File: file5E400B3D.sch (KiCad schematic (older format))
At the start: 12 parts

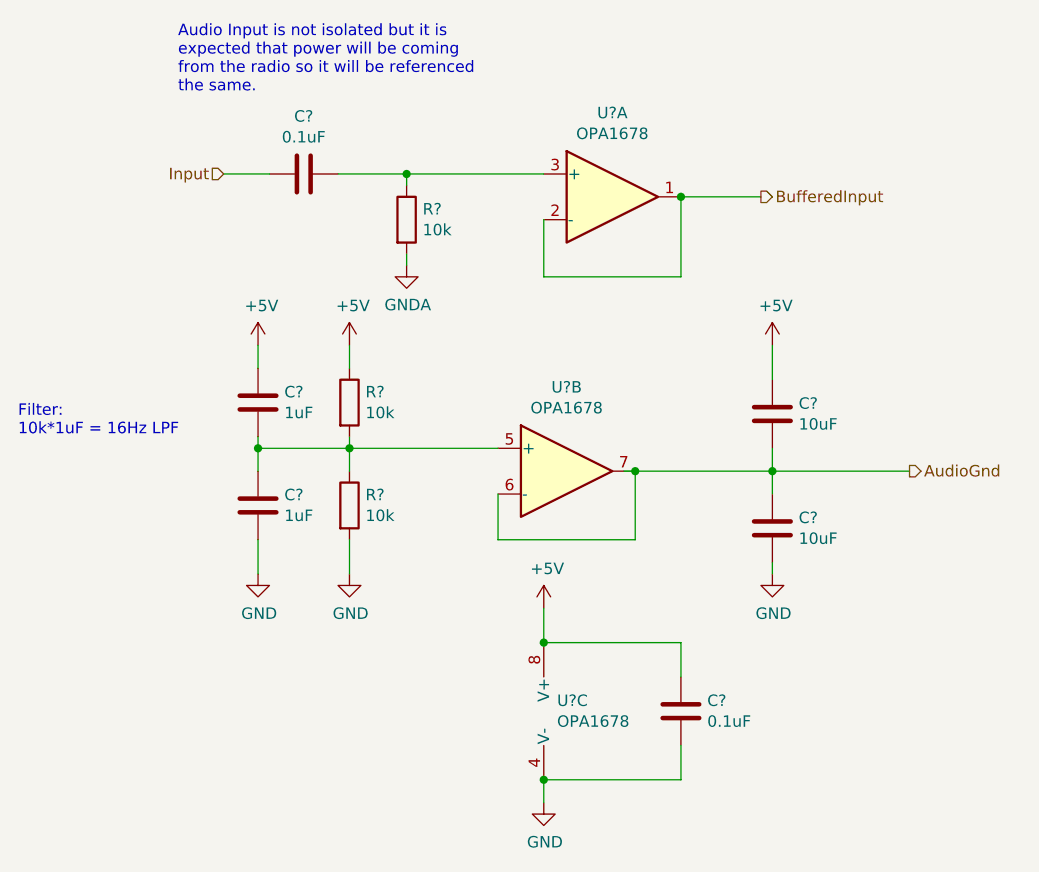
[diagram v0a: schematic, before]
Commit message: Ferrite beads and annotations
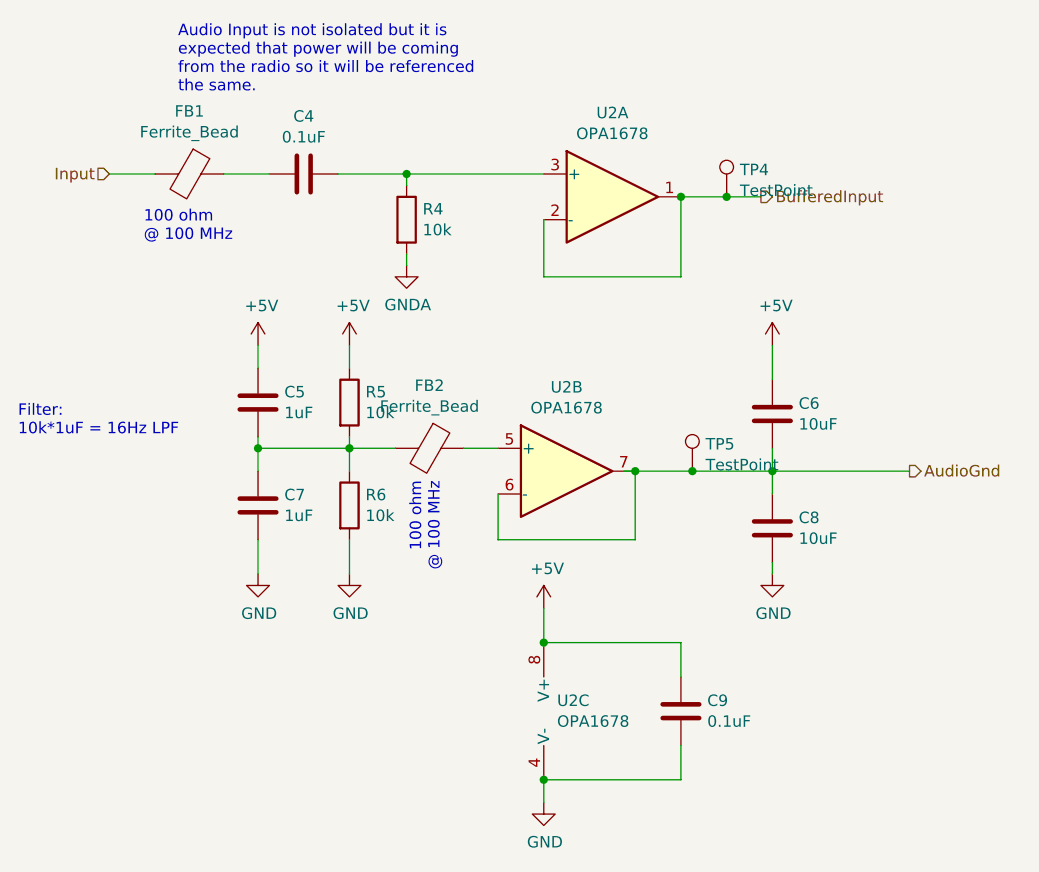
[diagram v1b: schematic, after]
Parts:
- added FB1, FB2: Ferrite_Bead, symbol Device:Ferrite_Bead
- added TP4, TP5: TestPoint, symbol Connector:TestPoint
- gave numbers to parts that had none: 10
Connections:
- wire segments 35 -> 39
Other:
- note added: "100 ohm \n@ 100 MHz"
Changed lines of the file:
@@
 Text HLabel 5900 2600 2    50   Output ~ 0
 BufferedInput
-Text HLabel 3550 2500 0    50   Input ~ 0
+Text HLabel 3050 2500 0    50   Input ~ 0
 Input
 Text HLabel 6550 3800 2    50   Output ~ 0
 AudioGnd
 $Comp
-L Device:R R?
+L Device:R R5
 U 1 1 5E400C47
 P 4100 3500
-F 0 "R?" H 4170 3546 50  0000 L CNN
+F 0 "R5" H 4170 3546 50  0000 L CNN
 F 1 "10k" H 4170 3455 50  0000 L CNN
 F 2 "" V 4030 3500 50  0001 C CNN
@@
 $EndComp
 $Comp
-L Device:R R?
+L Device:R R6
 U 1 1 5E400F84
 P 4100 3950
-F 0 "R?" H 4170 3996 50  0000 L CNN
+F 0 "R6" H 4170 3996 50  0000 L CNN
 F 1 "10k" H 4170 3905 50  0000 L CNN
 F 2 "" V 4030 3950 50  0001 C CNN
@@
 	4100 3650 4100 3700
 $Comp
-L power:+5V #PWR?
+L power:+5V #PWR015
 U 1 1 5E401BE8
 P 4100 3250
-F 0 "#PWR?" H 4100 3100 50  0001 C CNN
+F 0 "#PWR015" H 4100 3100 50  0001 C CNN
 F 1 "+5V" H 4115 3423 50  0000 C CNN
 F 2 "" H 4100 3250 50  0001 C CNN
@@
 $EndComp
 $Comp
-L power:GND #PWR?
+L power:GND #PWR018
 U 1 1 5E4020B9
 P 4100 4250
-F 0 "#PWR?" H 4100 4000 50  0001 C CNN
+F 0 "#PWR018" H 4100 4000 50  0001 C CNN
 F 1 "GND" H 4105 4077 50  0000 C CNN
 F 2 "" H 4100 4250 50  0001 C CNN
@@
 	4100 4250 4100 4100
 $Comp
-L Amplifier_Operational:OPA1678 U?
+L Amplifier_Operational:OPA1678 U2
 U 2 1 5E4026CE
 P 5050 3800
-F 0 "U?" H 5050 4167 50  0000 C CNN
+F 0 "U2" H 5050 4167 50  0000 C CNN
 F 1 "OPA1678" H 5050 4076 50  0000 C CNN
 F 2 "" H 5050 3800 50  0001 C CNN
@@
 $EndComp
 $Comp
-L Amplifier_Operational:OPA1678 U?
+L Amplifier_Operational:OPA1678 U2
 U 1 1 5E40401B
 P 5250 2600
-F 0 "U?" H 5250 2967 50  0000 C CNN
+F 0 "U2" H 5250 2967 50  0000 C CNN
 F 1 "OPA1678" H 5250 2876 50  0000 C CNN
 F 2 "" H 5250 2600 50  0001 C CNN
@@
 $EndComp
 $Comp
-L Amplifier_Operational:OPA1678 U?
+L Amplifier_Operational:OPA1678 U2
 U 3 1 5E405560
 P 5050 4850
-F 0 "U?" H 5008 4896 50  0000 L CNN
+F 0 "U2" H 5008 4896 50  0000 L CNN
 F 1 "OPA1678" H 5008 4805 50  0000 L CNN
 F 2 "" H 5050 4850 50  0001 C CNN
@@
 $EndComp
 $Comp
-L power:+5V #PWR?
+L power:+5V #PWR020
 U 1 1 5E406BA7
 P 4950 4400
-F 0 "#PWR?" H 4950 4250 50  0001 C CNN
+F 0 "#PWR020" H 4950 4250 50  0001 C CNN
 F 1 "+5V" H 4965 4573 50  0000 C CNN
 F 2 "" H 4950 4400 50  0001 C CNN
@@
 $EndComp
 $Comp
-L power:GND #PWR?
+L power:GND #PWR021
 U 1 1 5E406FD4
 P 4950 5250
-F 0 "#PWR?" H 4950 5000 50  0001 C CNN
+F 0 "#PWR021" H 4950 5000 50  0001 C CNN
 F 1 "GND" H 4955 5077 50  0000 C CNN
 F 2 "" H 4950 5250 50  0001 C CNN
@@
 Wire Wire Line
 	4950 4550 4950 4400
-Wire Wire Line
-	4100 3700 4750 3700
 Connection ~ 4100 3700
 Wire Wire Line
@@
 Connection ~ 5350 3800
 Wire Wire Line
-	5550 2600 5900 2600
+	5550 2600 5750 2600
 Wire Wire Line
 	5550 2600 5550 2950
@@
 	4100 3350 4100 3250
 $Comp
-L Device:C C?
+L Device:C C4
 U 1 1 5E450E38
 P 3900 2500
-F 0 "C?" V 3648 2500 50  0000 C CNN
+F 0 "C4" V 3648 2500 50  0000 C CNN
 F 1 "0.1uF" V 3739 2500 50  0000 C CNN
 F 2 "" H 3938 2350 50  0001 C CNN
@@
 	3550 2500 3750 2500
 $Comp
-L power:GNDA #PWR?
+L power:GNDA #PWR013
 U 1 1 5E45287C
 P 4350 2900
-F 0 "#PWR?" H 4350 2650 50  0001 C CNN
+F 0 "#PWR013" H 4350 2650 50  0001 C CNN
 F 1 "GNDA" H 4355 2727 50  0000 C CNN
 F 2 "" H 4350 2900 50  0001 C CNN
@@
 $EndComp
 $Comp
-L Device:C C?
+L Device:C C9
 U 1 1 5E45404C
 P 5550 4850
-F 0 "C?" H 5665 4896 50  0000 L CNN
+F 0 "C9" H 5665 4896 50  0000 L CNN
 F 1 "0.1uF" H 5665 4805 50  0000 L CNN
 F 2 "" H 5588 4700 50  0001 C CNN
@@
 Connection ~ 4950 5150
 $Comp
-L power:+5V #PWR?
+L power:+5V #PWR014
 U 1 1 5E45D063
 P 3700 3250
-F 0 "#PWR?" H 3700 3100 50  0001 C CNN
+F 0 "#PWR014" H 3700 3100 50  0001 C CNN
 F 1 "+5V" H 3715 3423 50  0000 C CNN
 F 2 "" H 3700 3250 50  0001 C CNN
@@
 $EndComp
 $Comp
-L power:GND #PWR?
+L power:GND #PWR017
 U 1 1 5E45D4E7
 P 3700 4250
-F 0 "#PWR?" H 3700 4000 50  0001 C CNN
+F 0 "#PWR017" H 3700 4000 50  0001 C CNN
 F 1 "GND" H 3705 4077 50  0000 C CNN
 F 2 "" H 3700 4250 50  0001 C CNN
@@
 $EndComp
 $Comp
-L Device:C C?
+L Device:C C5
 U 1 1 5E45DB74
 P 3700 3500
-F 0 "C?" H 3815 3546 50  0000 L CNN
+F 0 "C5" H 3815 3546 50  0000 L CNN
 F 1 "1uF" H 3815 3455 50  0000 L CNN
 F 2 "" H 3738 3350 50  0001 C CNN
@@
 $EndComp
 $Comp
-L Device:C C?
+L Device:C C7
 U 1 1 5E45EA2A
 P 3700 3950
-F 0 "C?" H 3815 3996 50  0000 L CNN
+F 0 "C7" H 3815 3996 50  0000 L CNN
 F 1 "1uF" H 3815 3905 50  0000 L CNN
 F 2 "" H 3738 3800 50  0001 C CNN
@@
 Filter:\n10k*1uF = 16Hz LPF
 $Comp
-L Device:C C?
+L Device:C C6
 U 1 1 5E464FDF
 P 5950 3550
-F 0 "C?" H 6065 3596 50  0000 L CNN
+F 0 "C6" H 6065 3596 50  0000 L CNN
 F 1 "10uF" H 6065 3505 50  0000 L CNN
 F 2 "" H 5988 3400 50  0001 C CNN
@@
 $EndComp
 $Comp
-L Device:C C?
+L Device:C C8
 U 1 1 5E4654FA
 P 5950 4050
-F 0 "C?" H 6065 4096 50  0000 L CNN
+F 0 "C8" H 6065 4096 50  0000 L CNN
 F 1 "10uF" H 6065 4005 50  0000 L CNN
 F 2 "" H 5988 3900 50  0001 C CNN
@@
 $EndComp
 $Comp
-L power:+5V #PWR?
+L power:+5V #PWR016
 U 1 1 5E469E13
 P 5950 3250
-F 0 "#PWR?" H 5950 3100 50  0001 C CNN
+F 0 "#PWR016" H 5950 3100 50  0001 C CNN
 F 1 "+5V" H 5965 3423 50  0000 C CNN
 F 2 "" H 5950 3250 50  0001 C CNN
@@
 $EndComp
 $Comp
-L power:GND #PWR?
+L power:GND #PWR019
 U 1 1 5E46A323
 P 5950 4250
-F 0 "#PWR?" H 5950 4000 50  0001 C CNN
+F 0 "#PWR019" H 5950 4000 50  0001 C CNN
 F 1 "GND" H 5955 4077 50  0000 C CNN
 F 2 "" H 5950 4250 50  0001 C CNN
@@
 	5950 3400 5950 3250
 Wire Wire Line
-	5350 3800 5950 3800
+	5350 3800 5600 3800
 Connection ~ 5950 3800
 Wire Wire Line
@@
 	4050 2500 4350 2500
 $Comp
-L Device:R R?
+L Device:R R4
 U 1 1 5E4A8F52
 P 4350 2700
-F 0 "R?" H 4420 2746 50  0000 L CNN
+F 0 "R4" H 4420 2746 50  0000 L CNN
 F 1 "10k" H 4420 2655 50  0000 L CNN
 F 2 "" V 4280 2700 50  0001 C CNN
@@
 Wire Wire Line
 	4350 2850 4350 2900
+$Comp
+L Device:Ferrite_Bead FB1
+U 1 1 5EC0D996
+P 3400 2500
+F 0 "FB1" V 3126 2500 50  0000 C CNN
+F 1 "Ferrite_Bead" V 3217 2500 50  0000 C CNN
+F 2 "" V 3330 2500 50  0001 C CNN
+F 3 "~" H 3400 2500 50  0001 C CNN
+	1    3400 2500
+	0    1    1    0
+$EndComp
+Wire Wire Line
+	3050 2500 3250 2500
+$Comp
+L Device:Ferrite_Bead FB2
+U 1 1 5EC0FD0A
+P 4450 3700
+F 0 "FB2" V 4176 3700 50  0000 C CNN
+F 1 "Ferrite_Bead" V 4267 3700 50  0000 C CNN
+F 2 "" V 4380 3700 50  0001 C CNN
+F 3 "~" H 4450 3700 50  0001 C CNN
+	1    4450 3700
+	0    1    1    0
+$EndComp
+Wire Wire Line
+	4600 3700 4750 3700
+Wire Wire Line
+	4300 3700 4100 3700
+Text Notes 3200 2800 0    50   ~ 0
+100 ohm \n@ 100 MHz
+Text Notes 4500 3850 3    50   ~ 0
+100 ohm \n@ 100 MHz
+$Comp
+L Connector:TestPoint TP4
+U 1 1 5EC17715
+P 5750 2600
+F 0 "TP4" H 5808 2718 50  0000 L CNN
+F 1 "TestPoint" H 5808 2627 50  0000 L CNN
+F 2 "" H 5950 2600 50  0001 C CNN
+F 3 "~" H 5950 2600 50  0001 C CNN
+	1    5750 2600
+	1    0    0    -1
+$EndComp
+Connection ~ 5750 2600
+Wire Wire Line
+	5750 2600 5900 2600
+$Comp
+L Connector:TestPoint TP5
+U 1 1 5EC17DFD
+P 5600 3800
+F 0 "TP5" H 5658 3918 50  0000 L CNN
+F 1 "TestPoint" H 5658 3827 50  0000 L CNN
+F 2 "" H 5800 3800 50  0001 C CNN
+F 3 "~" H 5800 3800 50  0001 C CNN
+	1    5600 3800
+	1    0    0    -1
+$EndComp
+Connection ~ 5600 3800
+Wire Wire Line
+	5600 3800 5950 3800
 $EndSCHEMATC

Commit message: Layout, 2020-05 order
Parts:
- C4, C5, C6, C7, C8, C9: footprint (none) -> Capacitors_SMD:C_0805_HandSoldering
- FB1, FB2: footprint (none) -> Inductors_SMD:L_0805_HandSoldering
- R4, R5, R6: footprint (none) -> Resistors_SMD:R_0805_HandSoldering
- TP4, TP5: footprint (none) -> Measurement_Points:Test_Point_Keystone_5000-5004_Miniature
- U2: footprint (none) -> SMD_Packages:SOIC-8-N
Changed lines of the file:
@@
 F 0 "R5" H 4170 3546 50  0000 L CNN
 F 1 "10k" H 4170 3455 50  0000 L CNN
-F 2 "" V 4030 3500 50  0001 C CNN
+F 2 "Resistors_SMD:R_0805_HandSoldering" V 4030 3500 50  0001 C CNN
 F 3 "~" H 4100 3500 50  0001 C CNN
 	1    4100 3500
@@
 F 0 "R6" H 4170 3996 50  0000 L CNN
 F 1 "10k" H 4170 3905 50  0000 L CNN
-F 2 "" V 4030 3950 50  0001 C CNN
+F 2 "Resistors_SMD:R_0805_HandSoldering" V 4030 3950 50  0001 C CNN
 F 3 "~" H 4100 3950 50  0001 C CNN
 	1    4100 3950
@@
 F 0 "U2" H 5050 4167 50  0000 C CNN
 F 1 "OPA1678" H 5050 4076 50  0000 C CNN
-F 2 "" H 5050 3800 50  0001 C CNN
+F 2 "SMD_Packages:SOIC-8-N" H 5050 3800 50  0001 C CNN
 F 3 "http://www.ti.com/lit/ds/symlink/opa1678.pdf" H 5050 3800 50  0001 C CNN
 	2    5050 3800
@@
 F 0 "U2" H 5250 2967 50  0000 C CNN
 F 1 "OPA1678" H 5250 2876 50  0000 C CNN
-F 2 "" H 5250 2600 50  0001 C CNN
+F 2 "SMD_Packages:SOIC-8-N" H 5250 2600 50  0001 C CNN
 F 3 "http://www.ti.com/lit/ds/symlink/opa1678.pdf" H 5250 2600 50  0001 C CNN
 	1    5250 2600
@@
 F 0 "U2" H 5008 4896 50  0000 L CNN
 F 1 "OPA1678" H 5008 4805 50  0000 L CNN
-F 2 "" H 5050 4850 50  0001 C CNN
+F 2 "SMD_Packages:SOIC-8-N" H 5050 4850 50  0001 C CNN
 F 3 "http://www.ti.com/lit/ds/symlink/opa1678.pdf" H 5050 4850 50  0001 C CNN
 	3    5050 4850
@@
 F 0 "C4" V 3648 2500 50  0000 C CNN
 F 1 "0.1uF" V 3739 2500 50  0000 C CNN
-F 2 "" H 3938 2350 50  0001 C CNN
+F 2 "Capacitors_SMD:C_0805_HandSoldering" H 3938 2350 50  0001 C CNN
 F 3 "~" H 3900 2500 50  0001 C CNN
 	1    3900 2500
@@
 F 0 "C9" H 5665 4896 50  0000 L CNN
 F 1 "0.1uF" H 5665 4805 50  0000 L CNN
-F 2 "" H 5588 4700 50  0001 C CNN
+F 2 "Capacitors_SMD:C_0805_HandSoldering" H 5588 4700 50  0001 C CNN
 F 3 "~" H 5550 4850 50  0001 C CNN
 	1    5550 4850
@@
 F 0 "C5" H 3815 3546 50  0000 L CNN
 F 1 "1uF" H 3815 3455 50  0000 L CNN
-F 2 "" H 3738 3350 50  0001 C CNN
+F 2 "Capacitors_SMD:C_0805_HandSoldering" H 3738 3350 50  0001 C CNN
 F 3 "~" H 3700 3500 50  0001 C CNN
 	1    3700 3500
@@
 F 0 "C7" H 3815 3996 50  0000 L CNN
 F 1 "1uF" H 3815 3905 50  0000 L CNN
-F 2 "" H 3738 3800 50  0001 C CNN
+F 2 "Capacitors_SMD:C_0805_HandSoldering" H 3738 3800 50  0001 C CNN
 F 3 "~" H 3700 3950 50  0001 C CNN
 	1    3700 3950
@@
 F 0 "C6" H 6065 3596 50  0000 L CNN
 F 1 "10uF" H 6065 3505 50  0000 L CNN
-F 2 "" H 5988 3400 50  0001 C CNN
+F 2 "Capacitors_SMD:C_0805_HandSoldering" H 5988 3400 50  0001 C CNN
 F 3 "~" H 5950 3550 50  0001 C CNN
 	1    5950 3550
@@
 F 0 "C8" H 6065 4096 50  0000 L CNN
 F 1 "10uF" H 6065 4005 50  0000 L CNN
-F 2 "" H 5988 3900 50  0001 C CNN
+F 2 "Capacitors_SMD:C_0805_HandSoldering" H 5988 3900 50  0001 C CNN
 F 3 "~" H 5950 4050 50  0001 C CNN
 	1    5950 4050
@@
 F 0 "R4" H 4420 2746 50  0000 L CNN
 F 1 "10k" H 4420 2655 50  0000 L CNN
-F 2 "" V 4280 2700 50  0001 C CNN
+F 2 "Resistors_SMD:R_0805_HandSoldering" V 4280 2700 50  0001 C CNN
 F 3 "~" H 4350 2700 50  0001 C CNN
 	1    4350 2700
@@
 F 0 "FB1" V 3126 2500 50  0000 C CNN
 F 1 "Ferrite_Bead" V 3217 2500 50  0000 C CNN
-F 2 "" V 3330 2500 50  0001 C CNN
+F 2 "Inductors_SMD:L_0805_HandSoldering" V 3330 2500 50  0001 C CNN
 F 3 "~" H 3400 2500 50  0001 C CNN
 	1    3400 2500
@@
 F 0 "FB2" V 4176 3700 50  0000 C CNN
 F 1 "Ferrite_Bead" V 4267 3700 50  0000 C CNN
-F 2 "" V 4380 3700 50  0001 C CNN
+F 2 "Inductors_SMD:L_0805_HandSoldering" V 4380 3700 50  0001 C CNN
 F 3 "~" H 4450 3700 50  0001 C CNN
 	1    4450 3700
@@
 F 0 "TP4" H 5808 2718 50  0000 L CNN
 F 1 "TestPoint" H 5808 2627 50  0000 L CNN
-F 2 "" H 5950 2600 50  0001 C CNN
+F 2 "Measurement_Points:Test_Point_Keystone_5000-5004_Miniature" H 5950 2600 50  0001 C CNN
 F 3 "~" H 5950 2600 50  0001 C CNN
 	1    5750 2600
@@
 F 0 "TP5" H 5658 3918 50  0000 L CNN
 F 1 "TestPoint" H 5658 3827 50  0000 L CNN
-F 2 "" H 5800 3800 50  0001 C CNN
+F 2 "Measurement_Points:Test_Point_Keystone_5000-5004_Miniature" H 5800 3800 50  0001 C CNN
 F 3 "~" H 5800 3800 50  0001 C CNN
 	1    5600 3800
